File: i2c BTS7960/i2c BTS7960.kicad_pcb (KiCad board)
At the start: 4 copper layers, 123.2 x 50.2 mm, 128 parts, among them J1 power in, J10 Conn_01x02, J2 Conn_01x04, J3 jst, J4 Conn_01x04, J5 jst, J6 to qwiic breakout, J7 qwiic 1, J8 qwiic 2, J9 Conn_01x02, U1 74AHC244, U10 BTS7960B, U11 BTS7960B, U12 ISO1540, U13 LD1117S33, U2 BTS7960B, U3 BTS7960B, U4 BTS7960B, U5 PCA9685, U6 BTS7960B, U7 74AHC244, U8 BTS7960B, U9 BTS7960B, U90 mp1584 dcdc

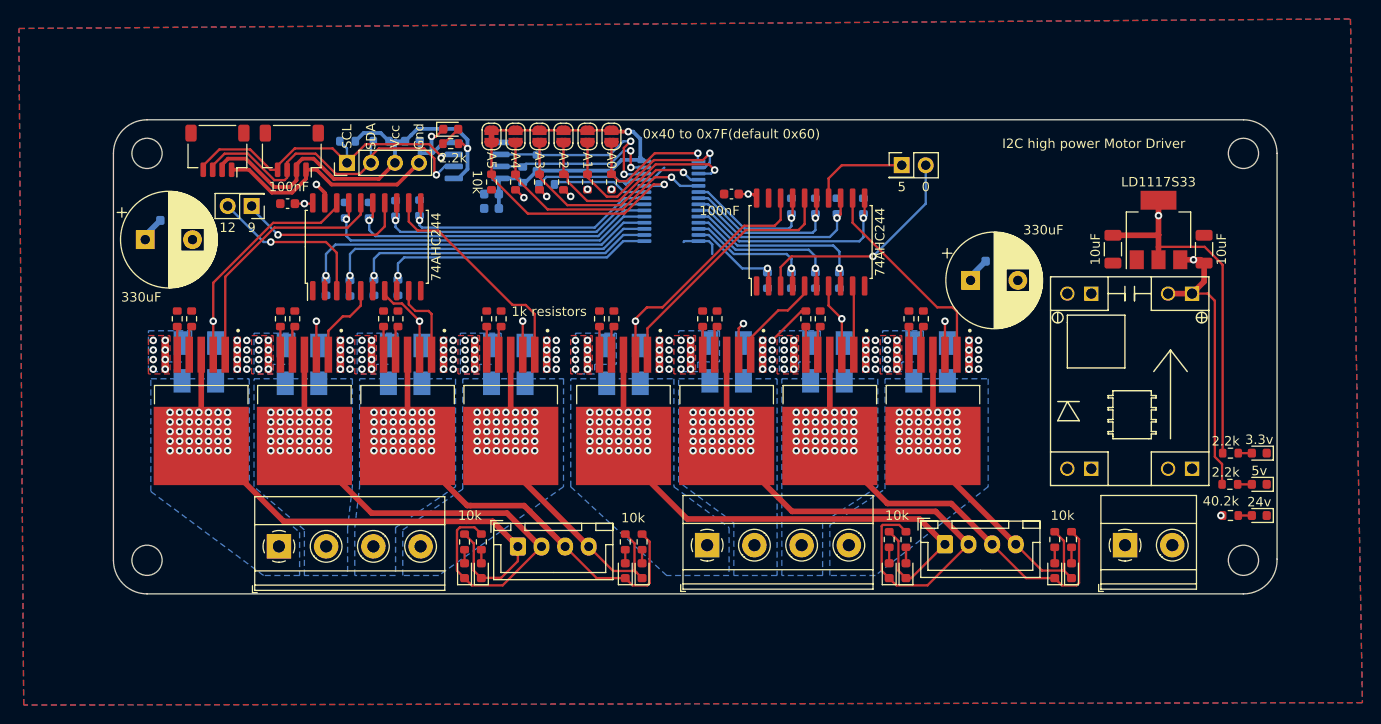
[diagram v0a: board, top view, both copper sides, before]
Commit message: motor controller DFM
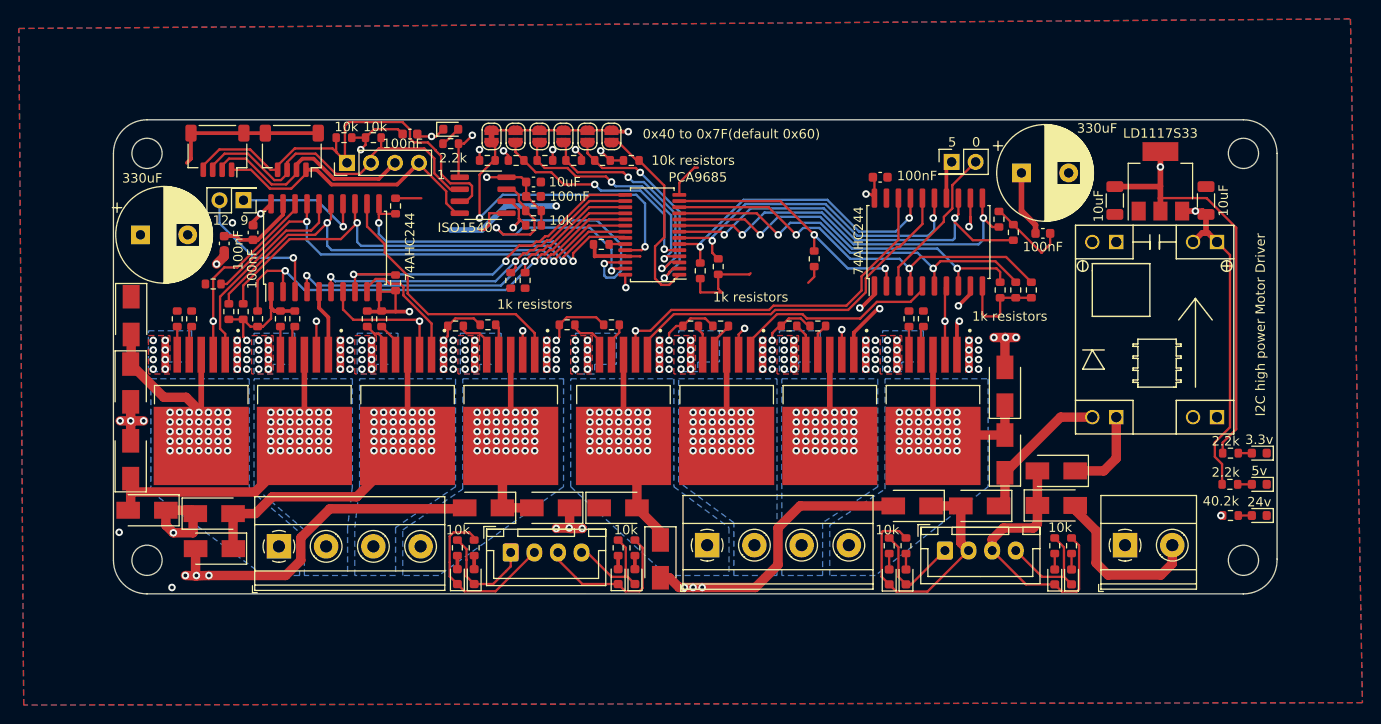
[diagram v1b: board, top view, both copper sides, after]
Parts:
- C1, C13, C2, C5, C9, R1, R2, R21, R22, R23, R24, R3, R39, R4, R5, R50, R51, R53, R54, R6, R7, R8, R84, R86, R88, R90, U12, U5: moved to F.Cu
- D1, D10, D11, D12, D13, D14, D15, D16, D2, D3, D4, D5, D6, D7, D8, D9: value DIODE -> type="D" model="DIODE" lib=""; moved to F.Cu
- moved D9 30.1 mm to (199.0, 122.6), turned to 0 degrees
- moved D6 29.3 mm to (190.9, 122.7), turned to 180 degrees
- moved D12 27.1 mm to (109.8, 123.5), turned to 0 degrees
- moved D11 26.8 mm to (109.9, 127.2), turned to 180 degrees
- moved D5 26.3 mm to (183.7, 122.7), turned to 180 degrees
- moved R1 25.4 mm to (196.3, 99.8)
- moved D10 25.2 mm to (199.0, 119.0), turned to 180 degrees
- moved D8 23.9 mm to (102.7, 123.1), turned to 180 degrees
- moved D1 21.4 mm to (157.1, 128.3), turned to -90 degrees
- moved R4 21.2 mm to (194.7, 99.8)
- moved R84 19.5 mm to (112.9, 102.1), turned to -90 degrees
- moved D7 19.2 mm to (101.0, 117.8)
- moved R8 18.9 mm to (194.4, 93.7)
- moved R21 18.6 mm to (142.7, 98.8)
- moved R23 18.3 mm to (111.4, 102.1), turned to -90 degrees
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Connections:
- J7 pad MP: (no net) -> GND
- J8 pad MP: (no net) -> GND
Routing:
- net GND: track 31.5 -> 185.7 mm, vias 70 -> 79
- net +24V: track 5.38 -> 105.7 mm, vias 65 -> 78
- net Net-(D11-A): track 44.7 -> 75.7 mm
- net +3V3: track 136.9 -> 167.4 mm, vias 2 -> 4
- net /pwm6: track 14.1 -> 44.1 mm, vias 1 -> 2
- net Net-(D19-K): track 57.8 -> 86.7 mm
- net /pwm5: track 17.0 -> 42.3 mm, vias 1 -> 2
- net Net-(D10-K): track 48.0 -> 72.6 mm
- net /pwm2: track 19.9 -> 43.8 mm, vias 1 -> 2
- net /pwm14: track 30.4 -> 51.7 mm, vias 1 -> 2
- net Net-(D23-K): track 58.8 -> 79.8 mm
- net /pwm4: track 20.1 -> 40.8 mm, vias 1 -> 2
- net /pwm13: track 33.6 -> 53.0 mm, vias 1 -> 2
- net /pwm1: track 17.4 -> 36.2 mm, vias 1 -> 2
- net /pwm3: track 23.2 -> 41.6 mm, vias 1 -> 2
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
